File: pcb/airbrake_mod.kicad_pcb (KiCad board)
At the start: 2 copper layers, 65.7 x 107.9 mm, 0 parts

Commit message: Change to 4 layer stackup
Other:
- copper layers 2 -> 4
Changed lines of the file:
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@@
 	(layers
 		(0 "F.Cu" signal)
+		(4 "In1.Cu" signal)
+		(6 "In2.Cu" signal)
 		(2 "B.Cu" signal)
 		(9 "F.Adhes" user "F.Adhesive")
@@
 	)
 	(setup
+		(stackup
+			(layer "F.SilkS"
+				(type "Top Silk Screen")
+			)
+			(layer "F.Paste"
+				(type "Top Solder Paste")
+			)
+			(layer "F.Mask"
+				(type "Top Solder Mask")
+				(thickness 0.01)
+			)
+			(layer "F.Cu"
+				(type "copper")
+				(thickness 0.035)
+			)
+			(layer "dielectric 1"
+				(type "prepreg")
+				(thickness 0.1)
+				(material "FR4")
+				(epsilon_r 4.5)
+				(loss_tangent 0.02)
+			)
+			(layer "In1.Cu"
+				(type "copper")
+				(thickness 0.035)
+			)
+			(layer "dielectric 2"
+				(type "core")
+				(thickness 1.24)
+				(material "FR4")
+				(epsilon_r 4.5)
+				(loss_tangent 0.02)
+			)
+			(layer "In2.Cu"
+				(type "copper")
+				(thickness 0.035)
+			)
+			(layer "dielectric 3"
+				(type "prepreg")
+				(thickness 0.1)
+				(material "FR4")
+				(epsilon_r 4.5)
+				(loss_tangent 0.02)
+			)
+			(layer "B.Cu"
+				(type "copper")
+				(thickness 0.035)
+			)
+			(layer "B.Mask"
+				(type "Bottom Solder Mask")
+				(thickness 0.01)
+			)
+			(layer "B.Paste"
+				(type "Bottom Solder Paste")
+			)
+			(layer "B.SilkS"
+				(type "Bottom Silk Screen")
+			)
+			(copper_finish "None")
+			(dielectric_constraints no)
+		)
 		(pad_to_mask_clearance 0)
 		(allow_soldermask_bridges_in_footprints no)

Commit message: Start layout
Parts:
- added BZ1: CEM-1203(42), Buzzer_SameSky:Buzzer_SameSky_CEM-1203_42, F.Cu at (28.6, 163.2)
- added C1: 2.2u, Capacitor_SMD:C_0603_1608Metric, F.Cu at (141.4, 110.0)
- added C10: 100n, Capacitor_SMD:C_0603_1608Metric, F.Cu at (190.1, 70.2)
- added C11: 100n, Capacitor_SMD:C_0603_1608Metric, F.Cu at (190.1, 72.7)
- added C12: 1u, Capacitor_SMD:C_0603_1608Metric, F.Cu at (161.4, 62.8)
- added C13: 100n, Capacitor_SMD:C_0603_1608Metric, F.Cu at (172.4, 93.5)
- added C14: 100n, Capacitor_SMD:C_0603_1608Metric, F.Cu at (190.1, 80.2)
- added C15: 100n, Capacitor_SMD:C_0603_1608Metric, F.Cu at (161.4, 61.1)
- added C16: CL21A226MAYNNNE, Capacitor_SMD:C_0805_2012Metric, F.Cu at (190.9, 36.5)
- added C17: CL10B104KB8NNWC, Capacitor_SMD:C_0603_1608Metric, F.Cu at (190.8, 38.5)
- added C18: 100n, Capacitor_SMD:C_0603_1608Metric, F.Cu at (193.5, 42.3)
- added C19: 100n, Capacitor_SMD:C_0603_1608Metric, F.Cu at (90.1, 74.1)
- added C2: 2.2u, Capacitor_SMD:C_0603_1608Metric, F.Cu at (141.4, 112.5)
- added C20: 10p, Capacitor_SMD:C_0603_1608Metric, F.Cu at (196.5, 38.7)
- added C21: CL21A226MAYNNNE, Capacitor_SMD:C_0805_2012Metric, F.Cu at (190.9, 43.0)
- added C22: 100n, Capacitor_SMD:C_0603_1608Metric, F.Cu at (74.3, 75.8)
- added C23: 100n, Capacitor_SMD:C_0603_1608Metric, F.Cu at (167.2, 112.1)
- added C24: 100n, Capacitor_SMD:C_0603_1608Metric, F.Cu at (135.0, 150.0)
- added C25: 4.7u, Capacitor_SMD:C_0603_1608Metric, F.Cu at (135.0, 148.3)
- added C26: 100n, Capacitor_SMD:C_0603_1608Metric, F.Cu at (144.5, 151.2)
- added C27: 100n, Capacitor_SMD:C_0603_1608Metric, F.Cu at (144.5, 152.9)
- added C28: 100n, Capacitor_SMD:C_0603_1608Metric, F.Cu at (155.4, 148.6)
- added C29: 220n, Capacitor_SMD:C_0603_1608Metric, F.Cu at (152.9, 150.9)
- added C3: 4.7u, Capacitor_SMD:C_0603_1608Metric, F.Cu at (186.1, 70.2)
- added C30: 100n, Capacitor_SMD:C_0603_1608Metric, F.Cu at (157.2, 148.6)
- added C31: 10u, Capacitor_SMD:C_0603_1608Metric, F.Cu at (159.0, 148.6)
- added C4: 14p, Capacitor_SMD:C_0603_1608Metric, F.Cu at (136.3, 84.0)
- added C5: 100n, Capacitor_SMD:C_0603_1608Metric, F.Cu at (186.1, 75.2)
- added C6: 1u, Capacitor_SMD:C_0603_1608Metric, F.Cu at (163.4, 50.8)
- added C7: 100n, Capacitor_SMD:C_0603_1608Metric, F.Cu at (186.1, 80.2)
- added C8: 100n, Capacitor_SMD:C_0603_1608Metric, F.Cu at (161.7, 50.8)
- added C9: 14p, Capacitor_SMD:C_0603_1608Metric, F.Cu at (140.3, 79.0)
- added D1: SS12, Diode_SMD:D_SMA, F.Cu at (147.3, 22.9)
- added D2: B1911USD, LED_SMD:LED_0603_1608Metric, F.Cu at (35.4, 80.7)
- added D3: B38G3RGB, B38G3RGB:B38G3RGB-10D0003H2U1930_HVK, F.Cu at (18.4, 140.8)
- added D4: SS12, Diode_SMD:D_SMA, F.Cu at (38.4, 165.4)
- added D5: B38G3RGB, B38G3RGB:B38G3RGB-10D0003H2U1930_HVK, F.Cu at (18.2, 151.1)
- added FB1: BLM18AG601SN1D, Inductor_SMD:L_0603_1608Metric, F.Cu at (160.0, 50.8)
- added H1: MountingHole, MountingHole:MountingHole_3.2mm_M3, F.Cu at (100.0, 55.5)
- added H2: MountingHole, MountingHole:MountingHole_3.2mm_M3, F.Cu at (55.5, 100.0)
- added H3: MountingHole, MountingHole:MountingHole_3.2mm_M3, F.Cu at (100.0, 144.4)
- added J1: XT30PW-M, Connector_AMASS_XT:AMASS_XT30PW-M_1x02_P2.50mm_Horizontal, F.Cu at (98.5, 76.5)
- added J2: Same Sky UJ20-C-H-G-SMT-P16-TR, SAMESKY_UJ20-C-H-G-SMT-P16-TR:SAMESKY_UJ20-C-H-G-SMT-P16-TR, F.Cu at (18.2, 60.0)
- added J3: 0436500315, Connector_Molex:Molex_Micro-Fit_3.0_43650-0315_1x03_P3.00mm_Vertical, F.Cu at (78.0, 58.1)
- added J4: TC2030, Connector:Tag-Connect_TC2030-IDC-FP_2x03_P1.27mm_Vertical, F.Cu at (54.0, 56.5)
- added J5: CNC_Tech_3220-14-0100-00, Connector_CNC_Tech:CNC_Tech_3220-14-0100-00, F.Cu at (50.8, 45.7)
- added L1: AMPI0640ED2R2MT, L_Arlitech:L_Arlitech_AMPI0640ED2R2MT_6.6mm_7.1mm_2628_6671_Metric, F.Cu at (185.0, 39.5)
- added Q1: NTR4003N, Package_TO_SOT_SMD:SOT-23-3, F.Cu at (148.9, 32.2)
- added Q2: NTR4003N, Package_TO_SOT_SMD:SOT-23-3, F.Cu at (145.4, 32.2)
- added Q3: Si3407DV, Package_SO:TSOP-6_1.65x3.05mm_P0.95mm, F.Cu at (145.3, 26.6)
- added Q4: NTR4003N, Package_TO_SOT_SMD:SOT-23-3, F.Cu at (78.5, 63.9)
- added Q5: Si3407DV, Package_SO:TSOP-6_1.65x3.05mm_P0.95mm, F.Cu at (86.0, 63.8)
- added Q6: NTR4003N, Package_TO_SOT_SMD:SOT-23-3, F.Cu at (36.9, 161.7)
- added R1: 47, Resistor_SMD:R_0603_1608Metric, F.Cu at (194.1, 70.2)
- added R10: 100, Resistor_SMD:R_0603_1608Metric, F.Cu at (145.0, 29.3)
- added R11: 47k, Resistor_SMD:R_0603_1608Metric, F.Cu at (148.0, 26.2)
- added R12: 135k, Resistor_SMD:R_0603_1608Metric, F.Cu at (195.0, 38.7)
- added R13: 30k, Resistor_SMD:R_0603_1608Metric, F.Cu at (193.5, 38.7)
- added R14: PA0805FRE7W0R002L, Resistor_SMD:R_0805_2012Metric, F.Cu at (80.0, 75.8)
- added R15: 30k, Resistor_SMD:R_0603_1608Metric, F.Cu at (18.6, 79.6)
- added R16: 47k, Resistor_SMD:R_0603_1608Metric, F.Cu at (18.6, 82.1)
- added R17: 5.1k, Resistor_SMD:R_0603_1608Metric, F.Cu at (26.4, 57.5)
- added R18: 5.1k, Resistor_SMD:R_0603_1608Metric, F.Cu at (26.4, 62.5)
- added R19: 600, Resistor_SMD:R_0603_1608Metric, F.Cu at (26.2, 81.4)
- added R2: 47k, Resistor_SMD:R_0603_1608Metric, F.Cu at (160.8, 93.9)
- added R20: 22, Resistor_SMD:R_0603_1608Metric, F.Cu at (167.2, 114.6)
- added R21: 22, Resistor_SMD:R_0603_1608Metric, F.Cu at (167.2, 117.2)
- added R22: 22, Resistor_SMD:R_0603_1608Metric, F.Cu at (167.2, 119.7)
- added R23: 22, Resistor_SMD:R_0603_1608Metric, F.Cu at (167.2, 122.2)
- added R24: 22, Resistor_SMD:R_0603_1608Metric, F.Cu at (167.2, 124.7)
- added R25: 47k, Resistor_SMD:R_0603_1608Metric, F.Cu at (167.2, 127.2)
- added R26: 47k, Resistor_SMD:R_0603_1608Metric, F.Cu at (167.2, 129.7)
- added R27: 47k, Resistor_SMD:R_0603_1608Metric, F.Cu at (167.2, 132.2)
- added R28: 100, Resistor_SMD:R_0603_1608Metric, F.Cu at (73.8, 63.6)
- added R29: 47k, Resistor_SMD:R_0603_1608Metric, F.Cu at (75.5, 63.6)
- added R3: 100, Resistor_SMD:R_0603_1608Metric, F.Cu at (150.4, 28.5)
- added R30: 100, Resistor_SMD:R_0603_1608Metric, F.Cu at (81.5, 63.9)
- added R31: 47k, Resistor_SMD:R_0603_1608Metric, F.Cu at (83.3, 63.9)
- added R32: 430, Resistor_SMD:R_0603_1608Metric, F.Cu at (16.7, 138.1)
- added R33: 100, Resistor_SMD:R_0603_1608Metric, F.Cu at (41.5, 161.7)
- added R34: 330, Resistor_SMD:R_0603_1608Metric, F.Cu at (18.4, 138.1)
- added R35: 47k, Resistor_SMD:R_0603_1608Metric, F.Cu at (39.9, 161.7)
- added R36: 330, Resistor_SMD:R_0603_1608Metric, F.Cu at (20.1, 138.1)
- added R37: 430, Resistor_SMD:R_0603_1608Metric, F.Cu at (16.5, 148.4)
- added R38: 330, Resistor_SMD:R_0603_1608Metric, F.Cu at (18.2, 148.4)
- added R39: 330, Resistor_SMD:R_0603_1608Metric, F.Cu at (19.9, 148.4)
- added R4: 47k, Resistor_SMD:R_0603_1608Metric, F.Cu at (195.0, 42.3)
- added R5: 47k, Resistor_SMD:R_0603_1608Metric, F.Cu at (148.1, 29.3)
- added R6: 100, Resistor_SMD:R_0603_1608Metric, F.Cu at (148.1, 35.2)
- added R7: 82k, Resistor_SMD:R_0603_1608Metric, F.Cu at (87.1, 72.5)
- added R8: 47k, Resistor_SMD:R_0603_1608Metric, F.Cu at (90.2, 72.5)
- added R9: 47k, Resistor_SMD:R_0603_1608Metric, F.Cu at (145.1, 35.2)
- added S1: RDS4-8S-1012-73-RA-254-D-67, SW_SameSky_RDS4-8S-1012-73-RA-254-D-67:SW_RDS4-8S-1012-73-RA-254-D-67, F.Cu at (32.4, 138.5)
- added SW1: GSPTS0018, PTS815_SJM_250_SMTR_LFS:SW_Push_PTS815_SJM_250_SMTR_LFS, F.Cu at (156.8, 93.6)
- added SW2: GSPTS0018, PTS815_SJM_250_SMTR_LFS:SW_Push_PTS815_SJM_250_SMTR_LFS, F.Cu at (168.4, 93.7)
- added SW3: GSPTS0018, PTS815_SJM_250_SMTR_LFS:SW_Push_PTS815_SJM_250_SMTR_LFS, F.Cu at (50.2, 135.2)
- added SW4: GSPTS0018, PTS815_SJM_250_SMTR_LFS:SW_Push_PTS815_SJM_250_SMTR_LFS, F.Cu at (50.2, 140.3)
- added SW5: GSPTS0018, PTS815_SJM_250_SMTR_LFS:SW_Push_PTS815_SJM_250_SMTR_LFS, F.Cu at (50.2, 145.3)
- added SW6: GSPTS0018, PTS815_SJM_250_SMTR_LFS:SW_Push_PTS815_SJM_250_SMTR_LFS, F.Cu at (50.2, 150.4)
- added U1: STM32H730VBTx, Package_QFP:LQFP-100_14x14mm_P0.5mm, F.Cu at (73.0, 107.7)
- added U2: TPS561246DRLR, Package_TO_SOT_SMD:SOT-563, F.Cu at (190.7, 40.5)
- added U3: ZXCT180A4W5, Package_TO_SOT_SMD:SOT-23-5, F.Cu at (77.0, 75.8)
- added U4: USBLC6-2SC6, Package_TO_SOT_SMD:SOT-23-6, F.Cu at (27.0, 60.0)
- added U5: W25Q128JVS, Package_SO:SOIC-8_5.3x5.3mm_P1.27mm, F.Cu at (174.4, 114.3)
- added U6: LPS22DF, Package_LGA:ST_HLGA-10_2x2mm_P0.5mm_LayoutBorder3x2y, F.Cu at (135.1, 152.3)
- added U7: LSM6DSV80X, Package_LGA:LGA-14_3x2.5mm_P0.5mm_LayoutBorder3x4y, F.Cu at (144.4, 148.8)
- added U8: IIS2MDC, ST_IIS2MDC:LGA-12_2X2X0P7_STM, F.Cu at (152.9, 148.4)
- added Y1: ECS-160-12-33B2Q-JES-TR3, Crystal:Crystal_SMD_3225-4Pin_3.2x2.5mm, F.Cu at (135.1, 79.5)
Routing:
- added copper zone on In2.Cu, net +3V3
- added copper zone on In1.Cu, net GND

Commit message: Layout power
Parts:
- added TP1: RCUCTE, TestPoint_KOASpeer:TestPoint_Chip_RCUCTE_0603, F.Cu at (89.3, 59.9)
- added TP10: RCUCTE, TestPoint_KOASpeer:TestPoint_Chip_RCUCTE_0603, F.Cu at (105.7, 50.0)
- added TP11: RCUCTE, TestPoint_KOASpeer:TestPoint_Chip_RCUCTE_0603, F.Cu at (109.4, 50.0)
- added TP2: RCUCTE, TestPoint_KOASpeer:TestPoint_Chip_RCUCTE_0603, F.Cu at (78.7, 63.5)
- added TP3: RCUCTE, TestPoint_KOASpeer:TestPoint_Chip_RCUCTE_0603, F.Cu at (93.5, 74.0)
- added TP4: RCUCTE, TestPoint_KOASpeer:TestPoint_Chip_RCUCTE_0603, F.Cu at (82.8, 69.5)
- added TP5: RCUCTE, TestPoint_KOASpeer:TestPoint_Chip_RCUCTE_0603, F.Cu at (81.0, 63.5)
- added TP6: RCUCTE, TestPoint_KOASpeer:TestPoint_Chip_RCUCTE_0603, F.Cu at (97.7, 50.0)
- added TP7: RCUCTE, TestPoint_KOASpeer:TestPoint_Chip_RCUCTE_0603, F.Cu at (91.1, 74.0)
- added TP8: RCUCTE, TestPoint_KOASpeer:TestPoint_Chip_RCUCTE_0603, F.Cu at (92.6, 59.9)
- added TP9: RCUCTE, TestPoint_KOASpeer:TestPoint_Chip_RCUCTE_0603, F.Cu at (99.3, 64.3)
- moved C20 117.5 mm to (80.1, 54.9), turned to 90 degrees
- moved R12 114.4 mm to (81.8, 54.9), turned to 90 degrees
- moved R6 114.0 mm to (81.4, 51.7), turned to -90 degrees
- moved R13 111.3 mm to (83.4, 54.9), turned to -90 degrees
- moved C19 110.9 mm to (83.0, 51.7), turned to 90 degrees
- moved C16 107.4 mm to (85.7, 57.6), turned to 180 degrees
- moved C17 106.3 mm to (85.8, 55.6), turned to 180 degrees
- moved U2 105.6 mm to (85.9, 53.6), turned to 180 degrees
- moved C21 105.6 mm to (85.7, 51.1), turned to 180 degrees
- moved L1 94.2 mm to (91.8, 53.0), turned to 180 degrees
- moved R3 81.5 mm to (76.8, 63.5)
- moved R4 80.6 mm to (76.8, 66.8), turned to -90 degrees
- moved Q1 77.3 mm to (79.8, 66.8), turned to 0 degrees
- moved D1 76.6 mm to (79.6, 58.8), turned to 180 degrees
- moved R5 72.6 mm to (82.9, 67.0), turned to -90 degrees
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- renumbered C19 to C18, C18 to C19, R5 to R4, R6 to R5, R4 to R6, SW3 to SW4, SW4 to SW5, SW5 to SW6, SW6 to SW7
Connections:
- J2 pad A6: Net-(J2-D+-PadA6) -> /USB/USB_D+
- J2 pad A7: Net-(J2-D--PadA7) -> /USB/USB_D-
- J2 pad B6: Net-(J2-D+-PadA6) -> /USB/USB_D+
- J2 pad B7: Net-(J2-D--PadA7) -> /USB/USB_D-
- U1 pad 70: /MCU/USB_DM -> /USB/USB_D-
- U1 pad 71: /MCU/USB_DP -> /USB/USB_D+
- U4 pad 1: Net-(J2-D--PadA7) -> /USB/USB_D-
- U4 pad 3: Net-(J2-D+-PadA6) -> /USB/USB_D+
- U4 pad 4: /MCU/USB_DP -> /USB/USB_D+
- U4 pad 6: /MCU/USB_DM -> /USB/USB_D-
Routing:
- net /USB/USB_D+: track 0.00 -> 7.90 mm
- net /USB/USB_D-: track 0.00 -> 7.55 mm
- net Net-(J2-CC1): track 0.00 -> 6.72 mm
- net Net-(J2-CC2): track 0.00 -> 3.40 mm
- added copper zone on F.Cu, net +BATT
- added copper zone on F.Cu, net /Power/BATT_MEAS
- added copper zone on F.Cu, net /Power/BUCK_IN
- added copper zone on F.Cu, net /Servo/SERVO_PWR
- added copper zone on F.Cu, net GND
- added copper zone on F.Cu, net VBUS
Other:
- board text added: "3V3"
- board text added: "PWR"
- board text added: "SIG"

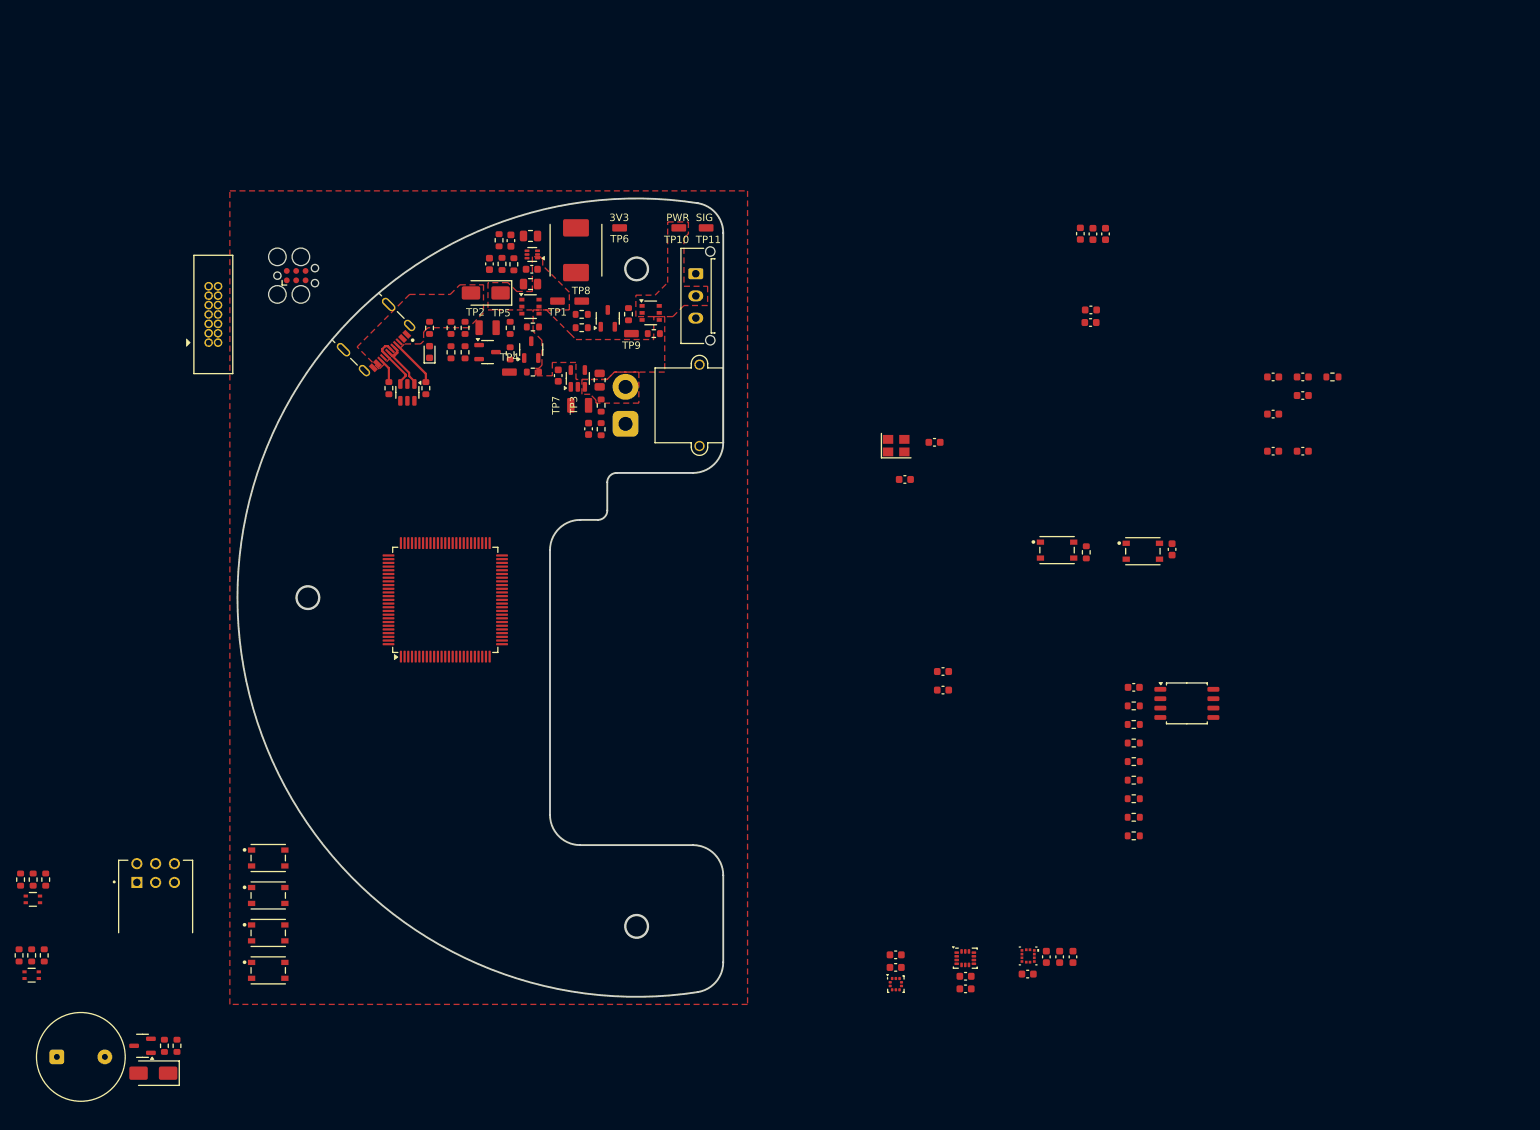
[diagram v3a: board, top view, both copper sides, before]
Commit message: Layout MCU decoupling
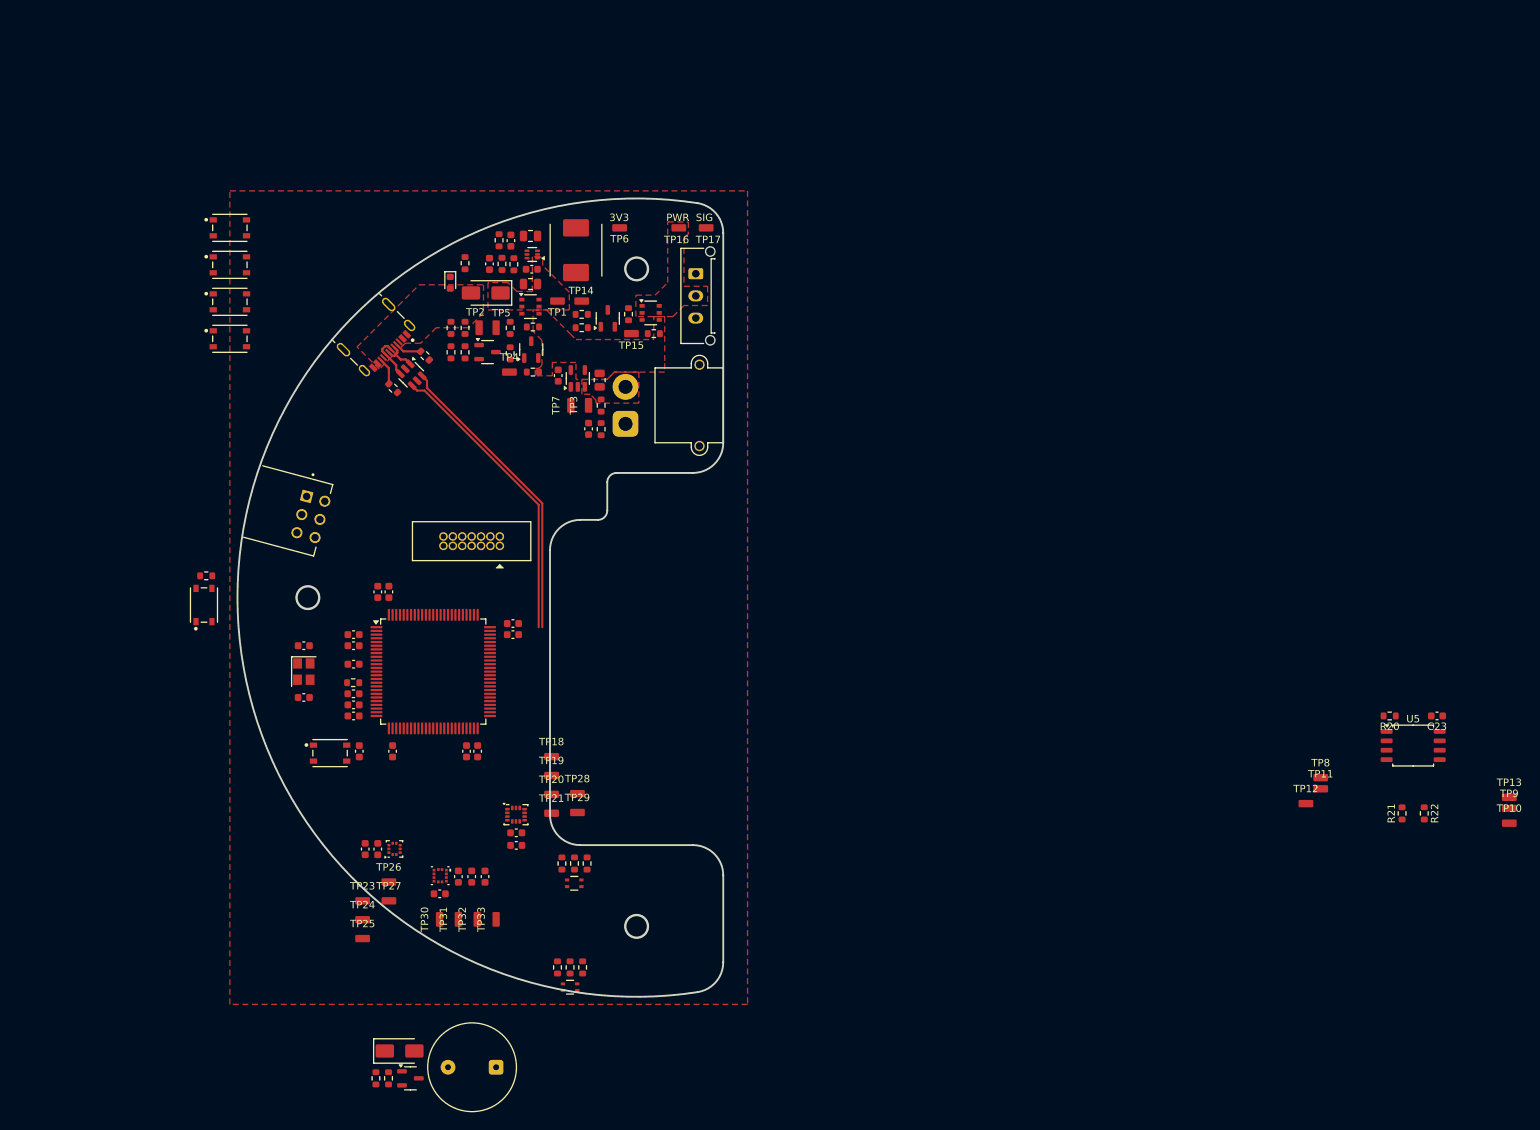
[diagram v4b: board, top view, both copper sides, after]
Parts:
- removed J4: TC2030, Connector:Tag-Connect_TC2030-IDC-FP_2x03_P1.27mm_Vertical
- removed the R23 at (167.2, 122.2)
- removed the R24 at (167.2, 124.7)
- removed the R25 at (167.2, 127.2)
- removed the R26 at (167.2, 129.7)
- removed the R27 at (167.2, 132.2)
- added TP10: RCUCTE, TestPoint_KOASpeer:TestPoint_Chip_RCUCTE_0603, F.Cu at (218.0, 130.5)
- added TP11: RCUCTE, TestPoint_KOASpeer:TestPoint_Chip_RCUCTE_0603, F.Cu at (192.5, 125.8)
- added TP12: RCUCTE, TestPoint_KOASpeer:TestPoint_Chip_RCUCTE_0603, F.Cu at (190.5, 127.8)
- added TP13: RCUCTE, TestPoint_KOASpeer:TestPoint_Chip_RCUCTE_0603, F.Cu at (218.0, 127.0)
- added TP18: RCUCTE, TestPoint_KOASpeer:TestPoint_Chip_RCUCTE_0603, F.Cu at (88.5, 121.5)
- added TP19: RCUCTE, TestPoint_KOASpeer:TestPoint_Chip_RCUCTE_0603, F.Cu at (88.5, 124.0)
- added TP20: RCUCTE, TestPoint_KOASpeer:TestPoint_Chip_RCUCTE_0603, F.Cu at (88.5, 126.6)
- added TP21: RCUCTE, TestPoint_KOASpeer:TestPoint_Chip_RCUCTE_0603, F.Cu at (88.5, 129.2)
- added TP23: RCUCTE, TestPoint_KOASpeer:TestPoint_Chip_RCUCTE_0603, F.Cu at (63.0, 141.0)
- added TP24: RCUCTE, TestPoint_KOASpeer:TestPoint_Chip_RCUCTE_0603, F.Cu at (63.0, 143.6)
- added TP25: RCUCTE, TestPoint_KOASpeer:TestPoint_Chip_RCUCTE_0603, F.Cu at (63.0, 146.1)
- added TP26: RCUCTE, TestPoint_KOASpeer:TestPoint_Chip_RCUCTE_0603, F.Cu at (66.5, 138.4)
- added TP27: RCUCTE, TestPoint_KOASpeer:TestPoint_Chip_RCUCTE_0603, F.Cu at (66.5, 141.0)
- added TP28: RCUCTE, TestPoint_KOASpeer:TestPoint_Chip_RCUCTE_0603, F.Cu at (92.0, 126.5)
- added TP29: RCUCTE, TestPoint_KOASpeer:TestPoint_Chip_RCUCTE_0603, F.Cu at (92.0, 129.1)
- added TP30: RCUCTE, TestPoint_KOASpeer:TestPoint_Chip_RCUCTE_0603, F.Cu at (73.3, 143.5)
- added TP31: RCUCTE, TestPoint_KOASpeer:TestPoint_Chip_RCUCTE_0603, F.Cu at (75.9, 143.5)
- added TP32: RCUCTE, TestPoint_KOASpeer:TestPoint_Chip_RCUCTE_0603, F.Cu at (78.5, 143.5)
- added TP33: RCUCTE, TestPoint_KOASpeer:TestPoint_Chip_RCUCTE_0603, F.Cu at (81.0, 143.5)
- added TP8: RCUCTE, TestPoint_KOASpeer:TestPoint_Chip_RCUCTE_0603, F.Cu at (192.5, 124.3)
- added TP9: RCUCTE, TestPoint_KOASpeer:TestPoint_Chip_RCUCTE_0603, F.Cu at (218.0, 128.5)
- R20, R21, R22: value 22 -> 47k
- moved R1 138.7 mm to (61.7, 111.5)
- moved C10 133.1 mm to (67.0, 120.8), turned to -90 degrees
- moved C7 127.6 mm to (61.7, 109.0), turned to 180 degrees
- moved C3 124.5 mm to (65.0, 99.2), turned to 90 degrees
- moved C5 122.0 mm to (66.5, 99.2), turned to 90 degrees
- moved C11 121.5 mm to (78.5, 120.8), turned to -90 degrees
- moved C6 120.0 mm to (61.7, 114.5), turned to 180 degrees
- moved C8 119.3 mm to (61.7, 116.0), turned to 180 degrees
- moved R2 119.0 mm to (41.8, 97.0), turned to 180 degrees
- moved FB1 116.3 mm to (61.7, 113.0), turned to 0 degrees
- moved SW1 115.6 mm to (41.5, 101.0), turned to 90 degrees
- moved C13 113.2 mm to (62.5, 120.8)
- moved SW2 113.2 mm to (58.5, 121.0)
- moved C15 109.6 mm to (61.7, 106.5), turned to 180 degrees
- moved C14 109.3 mm to (83.3, 103.5)
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- renumbered R28 to R23, R29 to R24, R30 to R25, R31 to R26, R32 to R27, R33 to R28, R34 to R29, R35 to R30, R36 to R31, R37 to R32, R38 to R33, R39 to R34, TP8 to TP14, TP9 to TP15, TP10 to TP16, TP11 to TP17
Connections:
- D2 pad 1: GND -> Net-(D2-K)
- D2 pad 2: Net-(D2-A) -> VBUS
- J2 pad A6: /USB/USB_D+ -> Net-(J2-D+-PadA6)
- J2 pad A7: /USB/USB_D- -> Net-(J2-D--PadA7)
- J2 pad B6: /USB/USB_D+ -> Net-(J2-D+-PadA6)
- J2 pad B7: /USB/USB_D- -> Net-(J2-D--PadA7)
- R19 pad 1: VBUS -> Net-(D2-K)
- R19 pad 2: Net-(D2-A) -> GND
- R20 pad 1: /Flash/CLK -> +3V3
- R20 pad 2: Net-(U5-CLK) -> /Flash/~{CS}
- R21 pad 1: /Flash/IO0 -> +3V3
- R21 pad 2: Net-(U5-DI/IO_{0}) -> /Flash/IO2
- R22 pad 1: /Flash/IO1 -> +3V3
- R22 pad 2: Net-(U5-DO/IO_{1}) -> /Flash/IO3
- U1 pad 70: /USB/USB_D- -> /MCU/USB_D-
- U1 pad 71: /USB/USB_D+ -> /MCU/USB_D+
- U4 pad 1: /USB/USB_D- -> Net-(J2-D--PadA7)
- U4 pad 3: /USB/USB_D+ -> Net-(J2-D+-PadA6)
- U4 pad 4: /USB/USB_D+ -> /MCU/USB_D+
- U4 pad 6: /USB/USB_D- -> /MCU/USB_D-
- U5 pad 2: Net-(U5-DO/IO_{1}) -> /Flash/IO1
- U5 pad 3: Net-(U5-~{WP}/IO_{2}) -> /Flash/IO2
- U5 pad 5: Net-(U5-DI/IO_{0}) -> /Flash/IO0
- U5 pad 6: Net-(U5-CLK) -> /Flash/CLK
- U5 pad 7: Net-(U5-~{HOLD}/~{RESET}/IO_{3}) -> /Flash/IO3
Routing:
- net /MCU/USB_D-: track 0.00 -> 40.7 mm
- net /MCU/USB_D+: track 0.00 -> 40.3 mm
- net /USB/USB_D+: track 7.90 -> 0.00 mm
- net /USB/USB_D-: track 7.55 -> 0.00 mm
- net Net-(J2-D+-PadA6): track 0.00 -> 5.94 mm
- net Net-(J2-D--PadA7): track 0.00 -> 4.98 mm
- net Net-(J2-CC1): track 6.72 -> 3.64 mm
